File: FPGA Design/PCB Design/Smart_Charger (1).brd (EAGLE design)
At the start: 108.3 x 65.5 mm, 104 parts, among them IC1 MID400, IC2 MID400, IC3 LMV358, IC4 LMV358, Q1 2222A, Q2 2222A

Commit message: changes
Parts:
- R11: device SparkFun:0603-RES -> SparkFun:0805

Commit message: dgsdg
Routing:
- net GND: track 59.5 -> 57.4 mm
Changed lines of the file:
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@@
 <contactref element="R31" pad="2"/>
 <contactref element="R32" pad="2"/>
-<wire x1="36.938478125" y1="53.24861875" x2="39.486878125" y2="53.24861875" width="0.254" layer="16"/>
 <contactref element="LEDS" pad="1"/>
 <contactref element="C10" pad="2"/>
@@
 <wire x1="115.691478125" y1="55.76161875" x2="110.611478125" y2="55.76161875" width="0.6096" layer="16"/>
 <wire x1="109.440278125" y1="35.26281875" x2="107.831478125" y2="36.87161875" width="0.4064" layer="1"/>
-<wire x1="35.87241875" y1="52.182559375" x2="34.681478125" y2="50.99161875" width="0.4064" layer="16"/>
-<wire x1="35.87241875" y1="52.182559375" x2="35.87241875" y2="52.34431875" width="0.4064" layer="16"/>
-<wire x1="35.87241875" y1="52.34431875" x2="36.034178125" y2="52.34431875" width="0.4064" layer="16"/>
-<wire x1="36.034178125" y1="52.34431875" x2="36.938478125" y2="53.24861875" width="0.4064" layer="16"/>
-<wire x1="34.681478125" y1="50.99161875" x2="34.681478125" y2="50.538059375" width="0.4064" layer="16"/>
-<wire x1="34.681478125" y1="50.538059375" x2="35.786059375" y2="49.433478125" width="0.4064" layer="16"/>
 <wire x1="114.520278125" y1="35.26281875" x2="115.451478125" y2="34.33161875" width="0.6096" layer="16"/>
 <contactref element="DC2" pad="2"/>
@@
 <contactref element="C6" pad="1"/>
 <contactref element="DC2" pad="4"/>
+<wire x1="39.486878125" y1="53.24861875" x2="36.938478125" y2="53.24861875" width="0.4064" layer="16"/>
+<wire x1="36.938478125" y1="53.24861875" x2="34.681478125" y2="50.99161875" width="0.4064" layer="16"/>
+<wire x1="108.071478125" y1="58.30161875" x2="103.061478125" y2="58.69161875" width="0" layer="19" extent="16-16"/>
+<wire x1="107.048878125" y1="46.13421875" x2="106.626659375" y2="47.7512375" width="0" layer="19" extent="16-16"/>
+<wire x1="107.831478125" y1="36.87161875" x2="108.243678125" y2="46.13421875" width="0" layer="19" extent="16-16"/>
+<wire x1="95.361478125" y1="52.64161875" x2="103.061478125" y2="58.69161875" width="0" layer="19" extent="16-16"/>
+<wire x1="72.071478125" y1="19.90161875" x2="110.281678125" y2="28.93761875" width="0" layer="19" extent="16-16"/>
+<wire x1="71.661478125" y1="18.04161875" x2="72.071478125" y2="19.90161875" width="0" layer="19" extent="16-16"/>
+<wire x1="69.611478125" y1="19.44161875" x2="71.661478125" y2="18.04161875" width="0" layer="19" extent="16-16"/>
+<wire x1="65.961478125" y1="20.59161875" x2="69.611478125" y2="19.44161875" width="0" layer="19" extent="16-16"/>
+<wire x1="65.211478125" y1="16.34161875" x2="65.961478125" y2="20.59161875" width="0" layer="19" extent="16-16"/>
+<wire x1="60.441478125" y1="15.87161875" x2="65.211478125" y2="16.34161875" width="0" layer="19" extent="16-16"/>
+<wire x1="59.512196875" y1="16.6523375" x2="60.441478125" y2="15.87161875" width="0" layer="19" extent="16-16"/>
+<wire x1="58.631478125" y1="15.77161875" x2="58.17361875" y2="16.908778125" width="0" layer="19" extent="1-16"/>
+<wire x1="58.511478125" y1="18.54161875" x2="58.315859375" y2="17.05101875" width="0" layer="19" extent="1-16"/>
+<wire x1="58.158740625" y1="10.12525" x2="58.631478125" y2="15.77161875" width="0" layer="19" extent="16-16"/>
+<wire x1="55.156096875" y1="8.42771875" x2="58.158740625" y2="10.12525" width="0" layer="19" extent="1-1"/>
+<wire x1="48.851478125" y1="2.75161875" x2="51.391478125" y2="2.75161875" width="0" layer="19" extent="1-1"/>
+<wire x1="51.344278125" y1="10.25681875" x2="55.156096875" y2="8.42771875" width="0" layer="19" extent="1-1"/>
+<wire x1="48.187971875" y1="13.169896875" x2="51.344278125" y2="10.25681875" width="0" layer="19" extent="16-16"/>
+<wire x1="46.264278125" y1="10.25681875" x2="48.187971875" y2="13.169896875" width="0" layer="19" extent="16-16"/>
+<wire x1="45.801478125" y1="7.97161875" x2="46.264278125" y2="10.25681875" width="0" layer="19" extent="16-16"/>
+<wire x1="68.318740625" y1="10.12525" x2="65.211478125" y2="16.34161875" width="0" layer="19" extent="16-16"/>
+<wire x1="70.481478125" y1="6.33161875" x2="68.318740625" y2="10.12525" width="0" layer="19" extent="16-16"/>
+<wire x1="38.601278125" y1="5.90041875" x2="45.801478125" y2="7.97161875" width="0" layer="19" extent="16-16"/>
+<wire x1="35.711478125" y1="8.54161875" x2="38.601278125" y2="5.90041875" width="0" layer="19" extent="16-16"/>
+<wire x1="33.911478125" y1="5.84161875" x2="35.711478125" y2="8.54161875" width="0" layer="19" extent="16-16"/>
+<wire x1="31.861478125" y1="4.24161875" x2="33.911478125" y2="5.84161875" width="0" layer="19" extent="16-16"/>
+<wire x1="28.861478125" y1="3.54161875" x2="31.861478125" y2="4.24161875" width="0" layer="19" extent="16-16"/>
+<wire x1="26.755278125" y1="14.36661875" x2="35.711478125" y2="8.54161875" width="0" layer="19" extent="16-16"/>
+<wire x1="26.755278125" y1="15.63661875" x2="26.755278125" y2="14.36661875" width="0" layer="19" extent="16-16"/>
+<wire x1="23.961478125" y1="15.59161875" x2="26.755278125" y2="15.63661875" width="0" layer="19" extent="16-16"/>
+<wire x1="20.561478125" y1="15.59161875" x2="23.961478125" y2="15.59161875" width="0" layer="19" extent="16-16"/>
+<wire x1="25.271478125" y1="20.16161875" x2="23.961478125" y2="15.59161875" width="0" layer="19" extent="16-16"/>
+<wire x1="13.3923375" y1="11.483659375" x2="20.561478125" y2="15.59161875" width="0" layer="19" extent="16-16"/>
+<wire x1="13.1383375" y1="3.863659375" x2="13.3923375" y2="11.483659375" width="0" layer="19" extent="1-1"/>
+<wire x1="25.301478125" y1="29.12161875" x2="25.271478125" y2="20.16161875" width="0" layer="19" extent="16-16"/>
+<wire x1="14.251478125" y1="32.12381875" x2="25.301478125" y2="29.12161875" width="0" layer="19" extent="16-16"/>
+<wire x1="36.911478125" y1="29.77161875" x2="25.301478125" y2="29.12161875" width="0" layer="19" extent="16-16"/>
+<wire x1="42.001478125" y1="29.77161875" x2="36.911478125" y2="29.77161875" width="0" layer="19" extent="1-1"/>
+<wire x1="49.961478125" y1="28.04161875" x2="42.001478125" y2="29.77161875" width="0" layer="19" extent="16-16"/>
+<wire x1="60.168678125" y1="31.79921875" x2="49.961478125" y2="28.04161875" width="0" layer="19" extent="16-16"/>
+<wire x1="20.991478125" y1="43.58161875" x2="14.251478125" y2="32.12381875" width="0" layer="19" extent="16-16"/>
+<wire x1="17.651478125" y1="49.59161875" x2="20.991478125" y2="43.58161875" width="0" layer="19" extent="16-16"/>
+<wire x1="17.551478125" y1="56.00161875" x2="17.651478125" y2="49.59161875" width="0" layer="19" extent="16-16"/>
+<wire x1="31.236478125" y1="42.89911875" x2="20.991478125" y2="43.58161875" width="0" layer="19" extent="16-16"/>
+<wire x1="34.681478125" y1="50.99161875" x2="31.236478125" y2="42.89911875" width="0" layer="19" extent="1-1"/>
+<wire x1="42.061478125" y1="53.27401875" x2="39.486878125" y2="53.24861875" width="0" layer="19" extent="16-16"/>
+<wire x1="44.783078125" y1="53.32561875" x2="42.061478125" y2="53.27401875" width="0" layer="19" extent="16-16"/>
+<wire x1="47.921478125" y1="58.68161875" x2="44.783078125" y2="53.32561875" width="0" layer="19" extent="16-16"/>
 </signal>
 <signal name="BUTTON3">

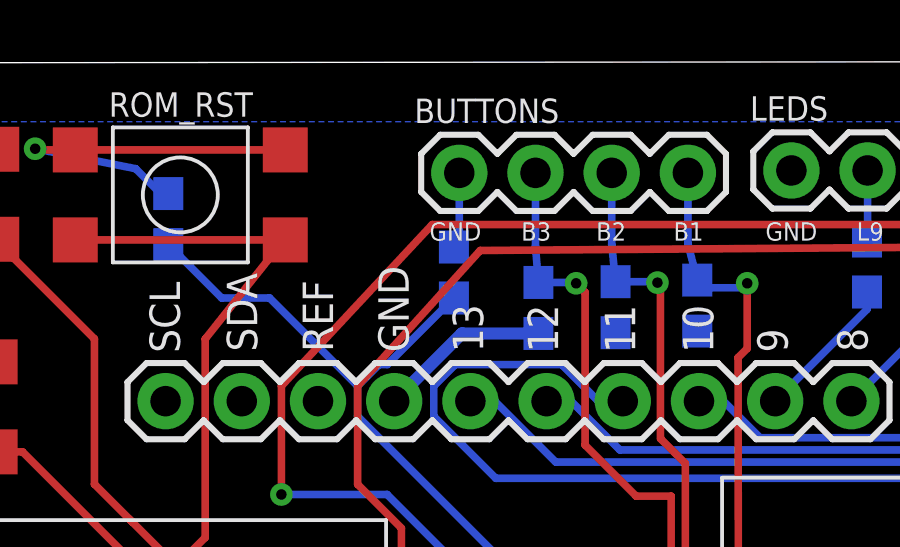
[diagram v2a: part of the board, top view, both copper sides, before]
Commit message: added smartenit eagle file
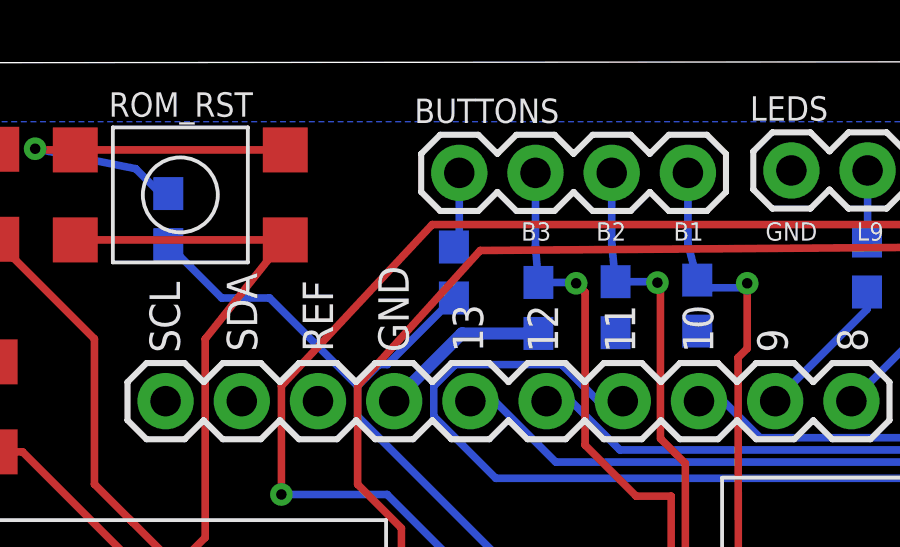
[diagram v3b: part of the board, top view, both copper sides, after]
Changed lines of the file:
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@@
 <text x="15.672565625" y="45.693834375" size="1.016" layer="21" font="vector" rot="R180">PILOT
  OUT</text>
-<text x="37.584371875" y="56.951878125" size="0.6096" layer="21" font="vector" rot="R180">GND</text>
 <text x="39.9110125" y="56.951878125" size="0.6096" layer="21" font="vector" rot="R180">B3</text>
 <text x="42.410371875" y="56.951878125" size="0.6096" layer="21" font="vector" rot="R180">B2</text>
